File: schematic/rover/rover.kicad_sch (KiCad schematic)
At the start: 0 parts

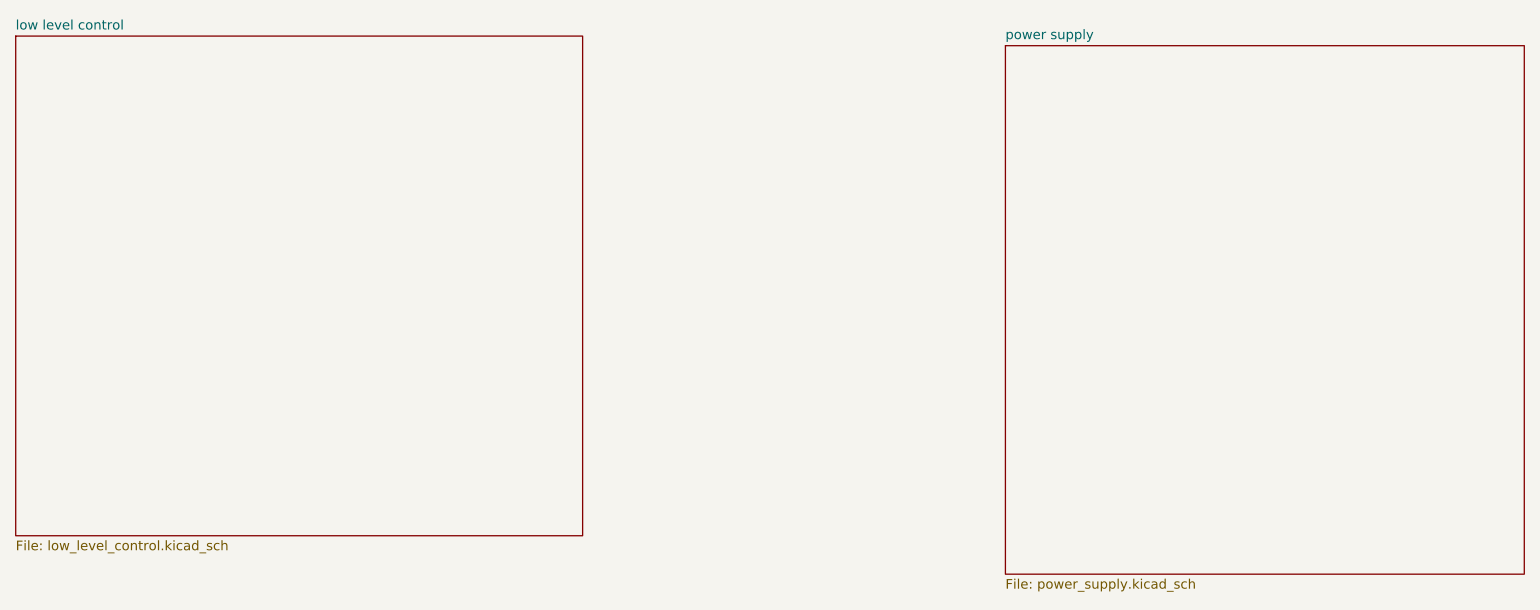
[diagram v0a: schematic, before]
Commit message: Complete power board and motor wiring
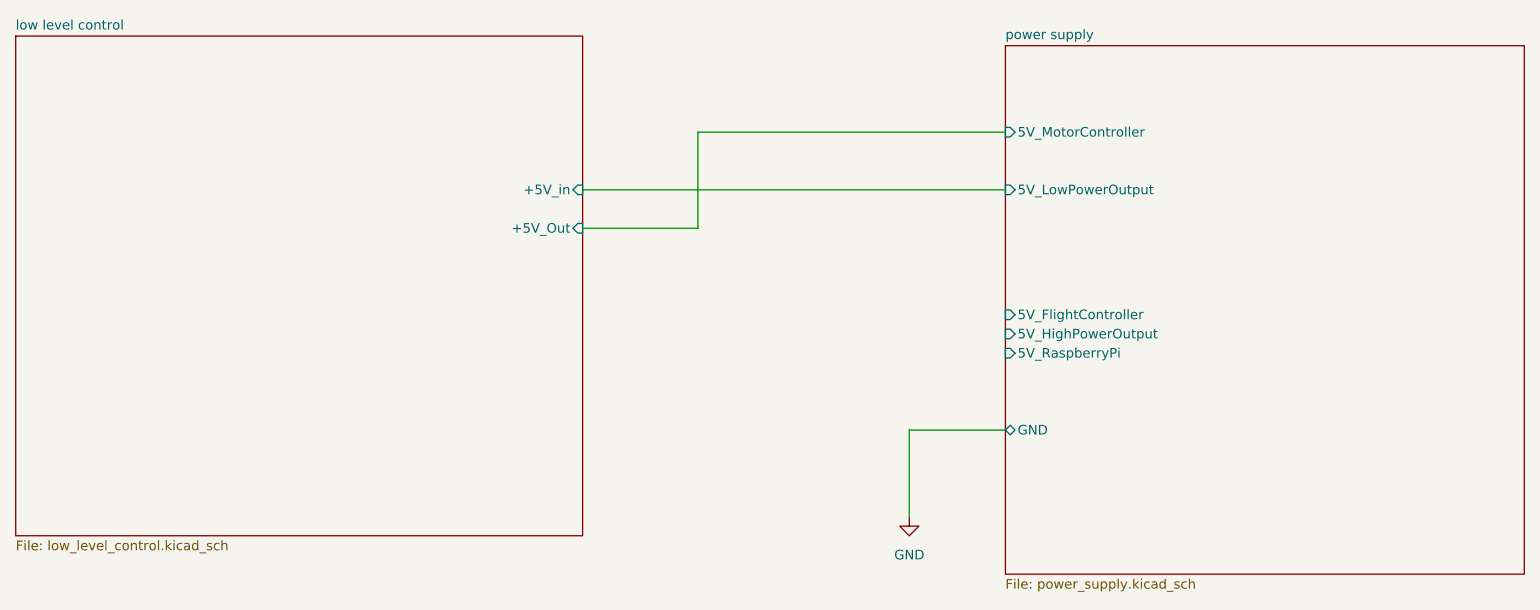
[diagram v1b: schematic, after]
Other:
- sheet low level control ports: added +5V_Out, +5V_in; removed none
- sheet power supply ports: added 5V_FlightController, 5V_HighPowerOutput, 5V_LowPowerOutput, 5V_MotorController, 5V_RaspberryPi, GND; removed none
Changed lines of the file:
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@@
 (kicad_sch (version 20230121) (generator eeschema)
   (paper "A4")
+  (wire (pts (xy 146.05 71.12) (xy 158.75 71.12))
+    (stroke (width 0) (type default))
+  )
+  (wire (pts (xy 102.87 39.37) (xy 158.75 39.37))
+    (stroke (width 0) (type default))
+  )
+  (wire (pts (xy 146.05 82.55) (xy 146.05 71.12))
+    (stroke (width 0) (type default))
+  )
+  (wire (pts (xy 118.11 31.75) (xy 118.11 44.45))
+    (stroke (width 0) (type default))
+  )
+  (wire (pts (xy 158.75 31.75) (xy 118.11 31.75))
+    (stroke (width 0) (type default))
+  )
+  (wire (pts (xy 118.11 44.45) (xy 102.87 44.45))
+    (stroke (width 0) (type default))
+  )
+  (symbol (lib_id "power:GND") (at 146.05 82.55 0) (unit 1)
+    (in_bom yes) (on_board yes) (dnp no) (fields_autoplaced)
+    (property "Reference" "#PWR013" (at 146.05 88.9 0)
+      (effects (font (size 1.27 1.27)) hide)
+    )
+    (property "Value" "GND" (at 146.05 87.63 0)
+      (effects (font (size 1.27 1.27)))
+    )
+    (property "Footprint" "" (at 146.05 82.55 0)
+      (effects (font (size 1.27 1.27)) hide)
+    )
+    (property "Datasheet" "" (at 146.05 82.55 0)
+      (effects (font (size 1.27 1.27)) hide)
+    )
+    (pin "1")
+    (instances
+      (project "rover"
+        (path "/e69e2e1e-a9af-4127-a558-2cc8fb636c94"
+          (reference "#PWR013") (unit 1)
+        )
+      )
+    )
+  )
   (sheet (at 158.75 20.32) (size 68.58 69.85) (fields_autoplaced)
     (stroke (width 0.1524) (type solid))
@@
     (property "Sheetfile" "power_supply.kicad_sch" (at 158.75 90.7546 0)
       (effects (font (size 1.27 1.27)) (justify left top))
+    )
+    (pin "5V_MotorController" input (at 158.75 31.75 180)
+      (effects (font (size 1.27 1.27)) (justify left))
+    )
+    (pin "GND" bidirectional (at 158.75 71.12 180)
+      (effects (font (size 1.27 1.27)) (justify left))
+    )
+    (pin "5V_LowPowerOutput" input (at 158.75 39.37 180)
+      (effects (font (size 1.27 1.27)) (justify left))
+    )
+    (pin "5V_HighPowerOutput" input (at 158.75 58.42 180)
+      (effects (font (size 1.27 1.27)) (justify left))
+    )
+    (pin "5V_RaspberryPi" input (at 158.75 60.96 180)
+      (effects (font (size 1.27 1.27)) (justify left))
+    )
+    (pin "5V_FlightController" input (at 158.75 55.88 180)
+      (effects (font (size 1.27 1.27)) (justify left))
     )
     (instances
@@
       (effects (font (size 1.27 1.27)) (justify left top))
     )
+    (pin "+5V_Out" input (at 102.87 44.45 0)
+      (effects (font (size 1.27 1.27)) (justify right))
+    )
+    (pin "+5V_in" input (at 102.87 39.37 0)
+      (effects (font (size 1.27 1.27)) (justify right))
+    )
     (instances
